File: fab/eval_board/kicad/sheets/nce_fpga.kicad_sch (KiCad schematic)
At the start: 2 parts, among them U1 NCE_TEST_CHIP, U2 XC7A100T

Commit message: fix: regenerate KiCad files in valid KiCad 8 format
- Rewrote all .kicad_sch files with proper lib_symbols sections,
  symbol instances, wires, hierarchical sheet references, and
  power port definitions (removed invalid ';;' comment syntax)
- Fixed .kicad_pcb: removed comment lines, added 922 missing net
  definitions, fixed gr_text justify format
- Regenerated Gerbers from fixed PCB using kicad-cli (30 files)
- All files validated with kicad-cli: schematic exports 5-page PDF,
  PCB exports SVG, DRC/ERC both run without parse errors
- Added regenerate_kicad.py generator script for reproducibility

Co-Authored-By: Bola Olatunji <bola.olatunji@ai.lightos.sh>
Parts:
- removed U1: NCE_TEST_CHIP, LightRail:QFN-64_8x8mm_P0.4mm, symbol LightRail:NCE_TEST_CHIP
- removed U2: XC7A100T, LightRail:BGA-256_14x14mm_P0.8mm, symbol FPGA_Xilinx_Artix7:XC7A100T-FTG256
- added C30, C31, C32, C33, C34, C35, C36, C37, C40, C41, C42, C43, C44, C45, C46, C47: 100nF, Capacitor_SMD:C_0402_1005Metric, symbol Device:C
- added J5: JTAG_2x5, Connector_PinHeader_2.54mm:PinHeader_2x05_P2.54mm_Vertical, symbol Connector_Generic:Conn_02x05
- added U1: NCE_Compute_Core, LightRail:QFN-64_8x8mm_P0.4mm, symbol LightRail:NCE_QFN64
- added U2: XC7A100T-1FTG256C, LightRail:BGA-256_14x14mm_P0.8mm, symbol FPGA_Xilinx:XC7A100T
- added U23: W25Q128JVSIQ, Package_SO:SOIC-8_3.9x4.9mm_P1.27mm, symbol Memory_Flash:W25Q128JVS
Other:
- note removed: "NCE Decoupling (near U1): 4x 100nF (0402) on VDD_CORE 4x 100nF (0402) on VDD_IO 2x 4.7uF (0402) bulk FPGA Decoupling (near U2): 8x 100nF (0402) VCCINT 4x 100nF (0402) VCCAUX 4x 4.7uF (0402) bulk 2x 10uF (0603) VCCO"
- title: NCE Test Chip + FPGA Controller — LightRail Eval Board -> NCE Test Chip + FPGA Controller - LightRail Eval Board

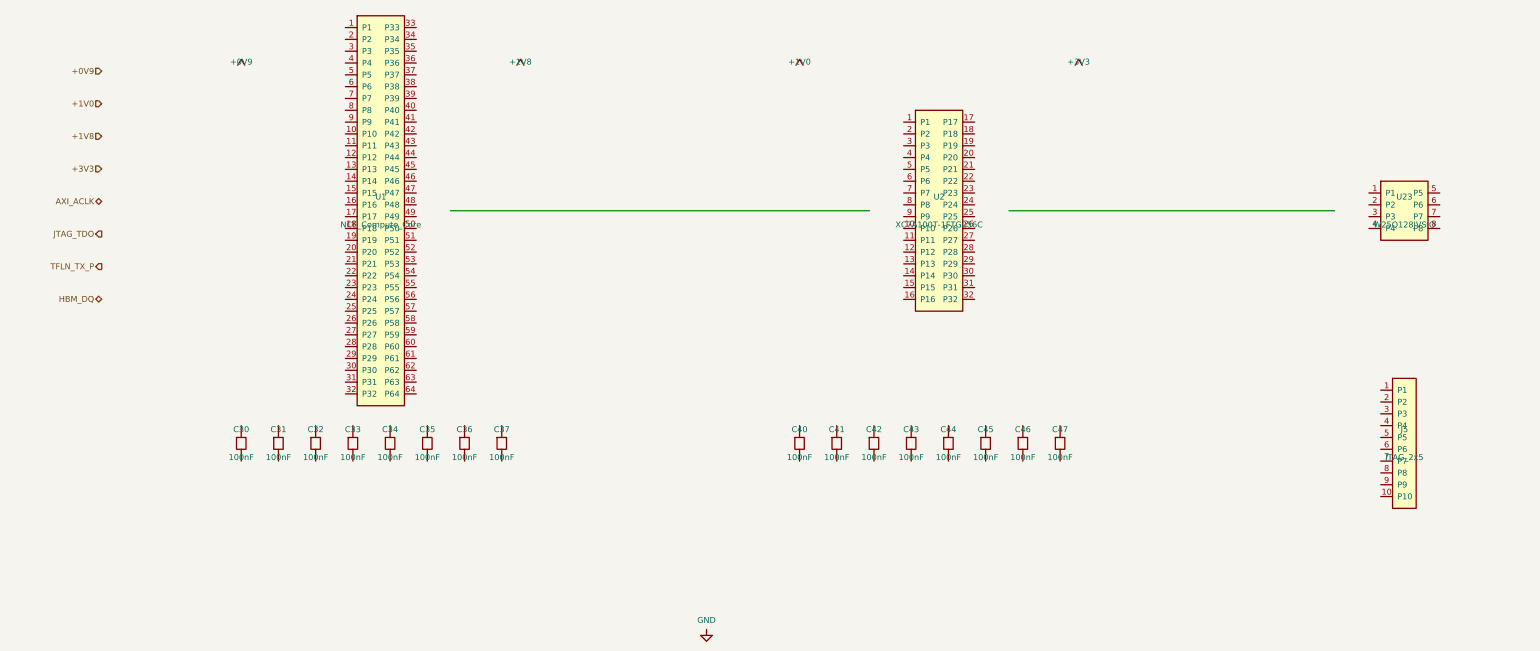
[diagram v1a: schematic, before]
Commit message: refactor: improve ERC quality via grid snapping and power flags
Co-Authored-By: Bola Olatunji <bola.olatunji@ai.lightos.sh>
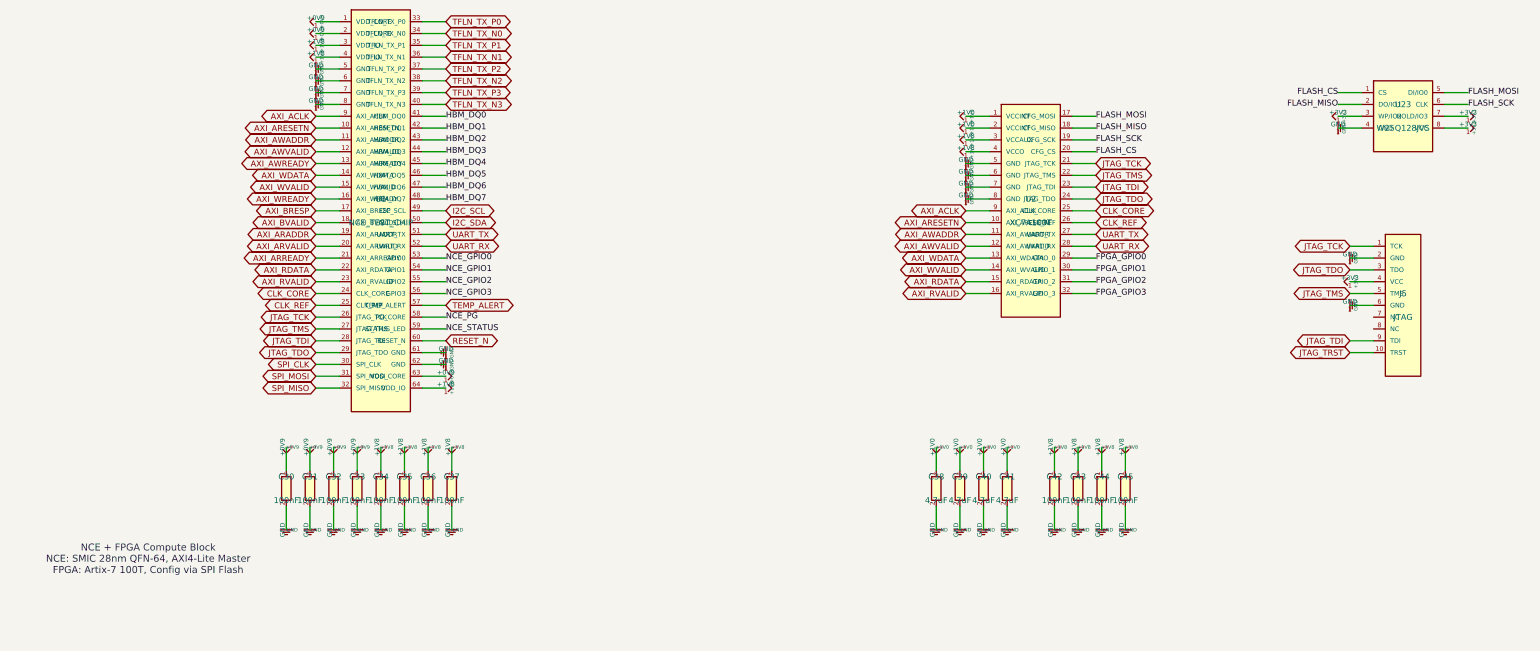
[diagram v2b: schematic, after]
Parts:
- removed C46, C47: 100nF, Capacitor_SMD:C_0402_1005Metric, symbol Device:C
- removed J5: JTAG_2x5, Connector_PinHeader_2.54mm:PinHeader_2x05_P2.54mm_Vertical, symbol Connector_Generic:Conn_02x05
- added C38, C39: 4.7uF, symbol Device:C
- added J5: JTAG, Connector_PinHeader_1.27mm:PinHeader_2x05_P1.27mm_Vertical, symbol Connector:JTAG_2x5
- C30, C31, C32, C33, C34, C35, C36, C37, C42, C43, C44, C45: footprint Capacitor_SMD:C_0402_1005Metric -> (none)
- C40, C41: value 100nF -> 4.7uF; footprint Capacitor_SMD:C_0402_1005Metric -> (none)
- U1: value NCE_Compute_Core -> NCE_TEST_CHIP; footprint LightRail:QFN-64_8x8mm_P0.4mm -> Package_DFN_QFN:QFN-64_8x8mm_P0.4mm; MPN LR-NCE-28-QFN64 -> LR-NCE-MPW-001
- U2: value XC7A100T-1FTG256C -> XC7A100T; footprint LightRail:BGA-256_14x14mm_P0.8mm -> Package_BGA:BGA-256_14x14mm_P0.8mm
- U23: value W25Q128JVSIQ -> W25Q128JVS; footprint Package_SO:SOIC-8_3.9x4.9mm_P1.27mm -> Package_SON:WSON-8_2x3mm
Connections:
- net +0V9: now also C30.1, C31.1, C32.1, C33.1, U1.1 (VDD_CORE), U1.2 (VDD_CORE), U1.63 (VDD_CORE)
- net +1V0: now also C40.1, C41.1, U2.1 (VCCINT), U2.2 (VCCINT), C38.1, C39.1
- net +1V8: now also C34.1, C35.1, C36.1, C37.1, C42.1, C43.1, C44.1, C45.1, U1.3 (VDD_IO), U1.4 (VDD_IO), U1.64 (VDD_IO), U2.3 (VCCAUX), U2.4 (VCCO)
- net +3V3: now also U23.3 (WP/IO2), U23.7 (HOLD/IO3), U23.8 (VCC), J5.4 (VCC)
- net AXI_ACLK: now also U1.9 (AXI_ACLK), U2.9 (AXI_ACLK)
- net GND: now also C30.2, C31.2, C32.2, C33.2, C34.2, C35.2, C36.2, C37.2, C40.2, C41.2, C42.2, C43.2, C44.2, C45.2, U1.5 (GND), U1.6 (GND), U1.61 (GND), U1.62 (GND), U1.7 (GND), U1.8 (GND), U2.5 (GND), U2.6 (GND), U2.7 (GND), U2.8 (GND), U23.4 (GND), C38.2, C39.2, J5.2 (GND), J5.6 (GND)
- net JTAG_TDO: now also U1.29 (JTAG_TDO), U2.24 (JTAG_TDO), J5.3 (TDO)
- net AXI_ARESETN: now reaches U2.10 (AXI_ARESETN)
- net AXI_ARESETN: now also U1.10 (AXI_ARESETN)
- net AXI_AWADDR: now reaches U2.11 (AXI_AWADDR)
- net AXI_AWADDR: now also U1.11 (AXI_AWADDR)
- net AXI_AWVALID: now reaches U2.12 (AXI_AWVALID)
- net AXI_AWVALID: now also U1.12 (AXI_AWVALID)
- net AXI_WDATA: now reaches U2.13 (AXI_WDATA)
- net AXI_WDATA: now also U1.14 (AXI_WDATA)
- net AXI_WVALID: now reaches U2.14 (AXI_WVALID)
- net AXI_WVALID: now also U1.15 (AXI_WVALID)
- net AXI_RDATA: now reaches U2.15 (AXI_RDATA)
- net AXI_RDATA: now also U1.22 (AXI_RDATA)
- net AXI_RVALID: now reaches U2.16 (AXI_RVALID)
- net AXI_RVALID: now also U1.23 (AXI_RVALID)
- net FLASH_MOSI: now reaches U2.17 (CFG_MOSI)
- net FLASH_MOSI: now also U23.5 (DI/IO0)
- net FLASH_MISO: now reaches U2.18 (CFG_MISO)
- net FLASH_MISO: now also U23.2 (DO/IO1)
- net FLASH_SCK: now reaches U2.19 (CFG_SCK)
- net FLASH_SCK: now also U23.6 (CLK)
- net FLASH_CS: now reaches U2.20 (CFG_CS)
- net FLASH_CS: now also U23.1 (CS)
- net JTAG_TCK: now reaches U2.21 (JTAG_TCK)
- net JTAG_TCK: now also U1.26 (JTAG_TCK), J5.1 (TCK)
- net JTAG_TMS: now reaches U2.22 (JTAG_TMS)
- net JTAG_TMS: now also U1.27 (JTAG_TMS), J5.5 (TMS)
- net JTAG_TDI: now reaches U2.23 (JTAG_TDI)
- net JTAG_TDI: now also U1.28 (JTAG_TDI), J5.9 (TDI)
- net CLK_CORE: now reaches U2.25 (CLK_CORE)
- net CLK_CORE: now also U1.24 (CLK_CORE)
- net CLK_REF: now reaches U2.26 (CLK_REF)
- net CLK_REF: now also U1.25 (CLK_REF)
- net UART_TX: now reaches U2.27 (UART_TX)
- net UART_TX: now also U1.51 (UART_TX)
- net UART_RX: now reaches U2.28 (UART_RX)
- net UART_RX: now also U1.52 (UART_RX)
- net FPGA_GPIO0: now reaches U2.29 (GPIO_0)
- net FPGA_GPIO1: now reaches U2.30 (GPIO_1)
- net FPGA_GPIO2: now reaches U2.31 (GPIO_2)
- net FPGA_GPIO3: now reaches U2.32 (GPIO_3)
- net AXI_AWREADY: now reaches U1.13 (AXI_AWREADY)
- net AXI_WREADY: now reaches U1.16 (AXI_WREADY)
- net AXI_BRESP: now reaches U1.17 (AXI_BRESP)
- net AXI_BVALID: now reaches U1.18 (AXI_BVALID)
- net AXI_ARADDR: now reaches U1.19 (AXI_ARADDR)
- net AXI_ARVALID: now reaches U1.20 (AXI_ARVALID)
- net AXI_ARREADY: now reaches U1.21 (AXI_ARREADY)
- net SPI_CLK: now reaches U1.30 (SPI_CLK)
- net SPI_MOSI: now reaches U1.31 (SPI_MOSI)
- net SPI_MISO: now reaches U1.32 (SPI_MISO)
- net TFLN_TX_P0: now reaches U1.33 (TFLN_TX_P0)
- net TFLN_TX_N0: now reaches U1.34 (TFLN_TX_N0)
- net TFLN_TX_P1: now reaches U1.35 (TFLN_TX_P1)
- net TFLN_TX_N1: now reaches U1.36 (TFLN_TX_N1)
- net TFLN_TX_P2: now reaches U1.37 (TFLN_TX_P2)
- net TFLN_TX_N2: now reaches U1.38 (TFLN_TX_N2)
- net TFLN_TX_P3: now reaches U1.39 (TFLN_TX_P3)
- net TFLN_TX_N3: now reaches U1.40 (TFLN_TX_N3)
- net HBM_DQ0: now reaches U1.41 (HBM_DQ0)
- net HBM_DQ1: now reaches U1.42 (HBM_DQ1)
- net HBM_DQ2: now reaches U1.43 (HBM_DQ2)
- net HBM_DQ3: now reaches U1.44 (HBM_DQ3)
- net HBM_DQ4: now reaches U1.45 (HBM_DQ4)
- net HBM_DQ5: now reaches U1.46 (HBM_DQ5)
- net HBM_DQ6: now reaches U1.47 (HBM_DQ6)
- net HBM_DQ7: now reaches U1.48 (HBM_DQ7)
- net I2C_SCL: now reaches U1.49 (I2C_SCL)
- net I2C_SDA: now reaches U1.50 (I2C_SDA)
- net NCE_GPIO0: now reaches U1.53 (GPIO0)
- net NCE_GPIO1: now reaches U1.54 (GPIO1)
- net NCE_GPIO2: now reaches U1.55 (GPIO2)
- net NCE_GPIO3: now reaches U1.56 (GPIO3)
- net TEMP_ALERT: now reaches U1.57 (TEMP_ALERT)
- net NCE_PG: now reaches U1.58 (PG_CORE)
- net NCE_STATUS: now reaches U1.59 (STATUS_LED)
- net RESET_N: now reaches U1.60 (RESET_N)
- new net JTAG_TRST: J5.10 (TRST)
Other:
- note added: "NCE + FPGA Compute Block NCE: SMIC 28nm QFN-64, AXI4-Lite Master FPGA: Artix-7 100T, Config via SPI Flash"
- title: NCE Test Chip + FPGA Controller - LightRail Eval Board -> NCE + FPGA - LightRail Eval Board
